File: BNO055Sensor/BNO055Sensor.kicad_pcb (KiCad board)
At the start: 4 copper layers, 50 x 35 mm, 10 parts, among them J1 locked, U1 Adafruit_BNO055_breakout

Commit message: Turns template and sensor board into two layer boards
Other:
- copper layers 4 -> 2
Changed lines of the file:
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@@
 (kicad_pcb (version 20220331) (generator pcbnew)
   (general
-    (thickness 1.6)
+    (thickness 0.57)
   )
   (paper "A4")
   (layers
     (0 "F.Cu" mixed)
-    (1 "In1.Cu" power)
-    (2 "In2.Cu" power)
     (31 "B.Cu" mixed)
-    (32 "B.Adhes" user)
-    (33 "F.Adhes" user)
+    (32 "B.Adhes" user "B.Adhesive")
+    (33 "F.Adhes" user "F.Adhesive")
     (34 "B.Paste" user)
     (35 "F.Paste" user)
-    (36 "B.SilkS" user)
-    (37 "F.SilkS" user)
+    (36 "B.SilkS" user "B.Silkscreen")
+    (37 "F.SilkS" user "F.Silkscreen")
     (38 "B.Mask" user)
     (39 "F.Mask" user)
-    (40 "Dwgs.User" user)
-    (41 "Cmts.User" user)
-    (42 "Eco1.User" user)
-    (43 "Eco2.User" user)
+    (40 "Dwgs.User" user "User.Drawings")
+    (41 "Cmts.User" user "User.Comments")
+    (42 "Eco1.User" user "User.Eco1")
+    (43 "Eco2.User" user "User.Eco2")
     (44 "Edge.Cuts" user)
     (45 "Margin" user)
-    (46 "B.CrtYd" user)
-    (47 "F.CrtYd" user)
+    (46 "B.CrtYd" user "B.Courtyard")
+    (47 "F.CrtYd" user "F.Courtyard")
     (48 "B.Fab" user)
     (49 "F.Fab" user)
@@
       (layer "F.Cu" (type "copper") (thickness 0.035))
       (layer "dielectric 1" (type "prepreg") (thickness 0.48) (material "FR4") (epsilon_r 4.5) (loss_tangent 0.02))
-      (layer "In1.Cu" (type "copper") (thickness 0.035))
-      (layer "dielectric 2" (type "prepreg") (thickness 0.48) (material "FR4") (epsilon_r 4.5) (loss_tangent 0.02))
-      (layer "In2.Cu" (type "copper") (thickness 0.035))
-      (layer "dielectric 3" (type "core") (thickness 0.48) (material "FR4") (epsilon_r 4.5) (loss_tangent 0.02))
       (layer "B.Cu" (type "copper") (thickness 0.035))
       (layer "B.Mask" (type "Bottom Solder Mask") (thickness 0.01))

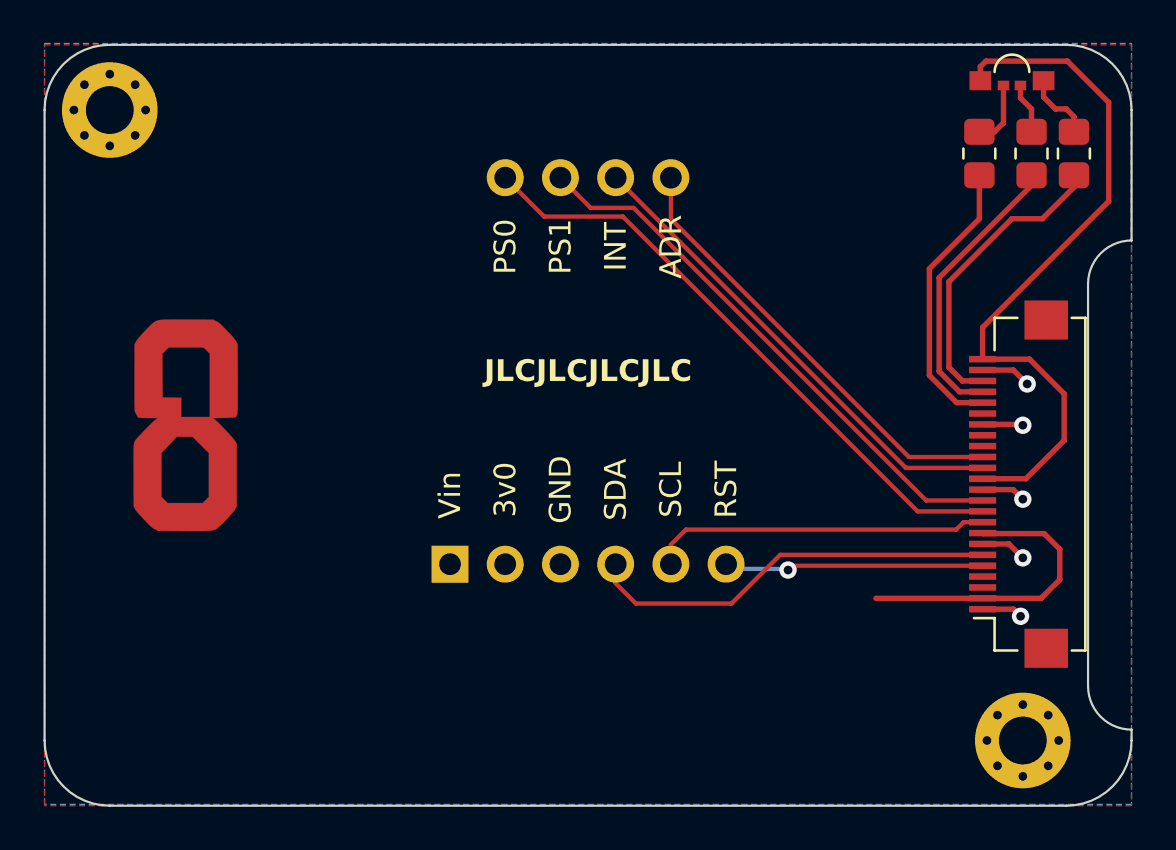
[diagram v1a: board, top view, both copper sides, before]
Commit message: Updates BNO055Sensor board after changes in the addon connector
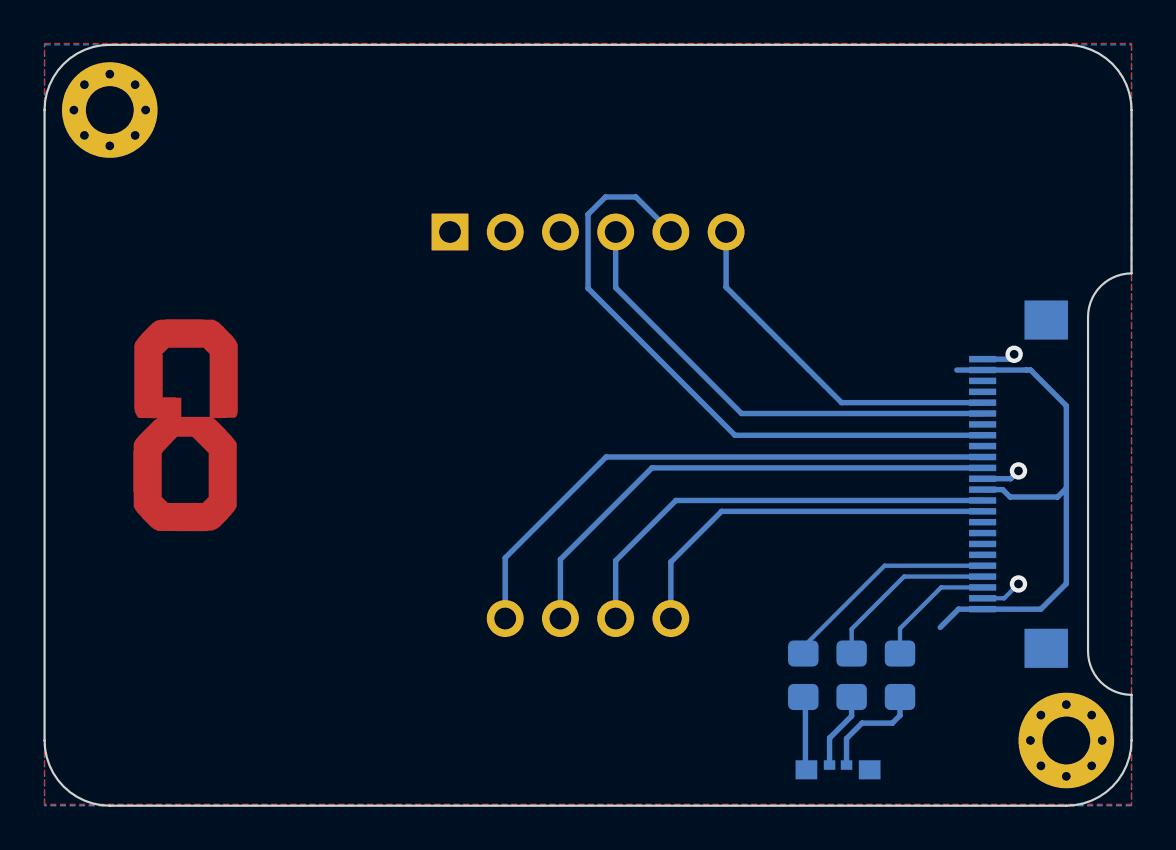
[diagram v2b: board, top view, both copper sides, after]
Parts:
- removed kibuzzard-6259E36C: G***, kibuzzard-6259E36C
- added kibuzzard-6282AB8D: G***, kibuzzard-6282AB8D, B.Cu at (122.5, 97.5)
- D1: value LED_RGBA -> LED_BGAR; moved to B.Cu
- J1: footprint GameOver:TXGA_FFC05036-24SBD113W5M_1x24_P0.50mm_Horizontal -> GameOver:Addon_conn_TXGA_FFC05036-24SBD113W5M_1x24_P0.50mm_Horizontal; moved to B.Cu
- R1, R2, R3, U1: moved to B.Cu
- moved D1 32.7 mm to (156.5, 113.3)
- moved R1 26.2 mm to (154.9, 109.0), turned to -90 degrees
- moved R3 25.3 mm to (159.3, 109.0), turned to -90 degrees
- moved R2 24.7 mm to (157.1, 109.0), turned to -90 degrees
- moved U1 5.04 mm to (145.0, 98.8)
- moved H2 2.00 mm to (167.0, 112.0)
- turned J1 to -90 degrees
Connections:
- D1 pad 1: Net-(D1-RK) -> Net-(D1-BK)
- D1 pad 3: Net-(D1-BK) -> +3V3
- D1 pad 4: +3V3 -> Net-(D1-RK)
- J1 pad 18: GND -> unconnected-(J1-IO25)
- J1 pad 20: LED_G -> LED_R
- J1 pad 21: LED_R -> LED_G
- J1 pad 7: GND -> unconnected-(J1-IO5)
- J1 pad 8: +3V3 -> SCL
- J1 pad 9: SCL -> unconnected-(J1-IO17)
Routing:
- net +3V3: track 46.8 -> 24.7 mm
- net SCL: track 15.7 -> 29.2 mm
- net LED_B: track 13.8 -> 5.73 mm
- net LED_G: track 13.1 -> 8.15 mm
- net GND: track 10.2 -> 5.27 mm, vias 5 -> 3
- net RST: track 12.0 -> 16.5 mm, vias 1 -> 0
- net LED_R: track 13.2 -> 10.1 mm
- net ADR: track 20.8 -> 17.9 mm
- net SDA: track 19.1 -> 21.8 mm
- net Net-(D1-BK): track 3.22 -> 4.97 mm
- net INT: track 22.4 -> 20.7 mm
- net PS1: track 25.6 -> 23.9 mm
- net PS0: track 28.3 -> 26.7 mm
- net Net-(D1-RK): track 2.34 -> 3.41 mm
- net Net-(D1-GK): track 3.00 -> 3.55 mm
- added copper zone on B.Cu, net +3V3
- added copper zone on F.Cu, net GND
- removed copper zone on F.Cu, net +3V3
- removed copper zone on B.Cu, net GND
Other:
- outline, holes or cut-outs redrawn

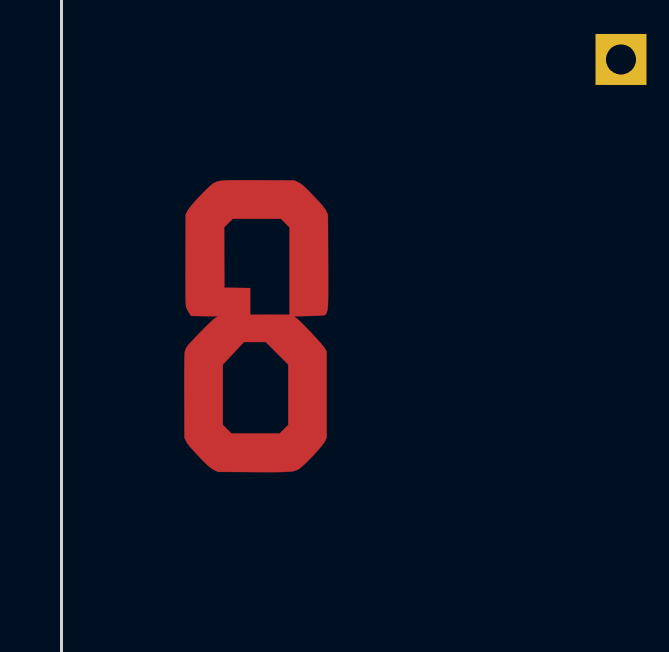
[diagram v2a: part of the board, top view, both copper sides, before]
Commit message: Fixes orientation for sensor board
The idea is to use the base board with the ESP32 facing down, and the
sensorboard with the sensor facing up. That way the connectors will face
each other correctly and the sensor will have space above (it wouldn't
fit between the boards because the battery will already be there).
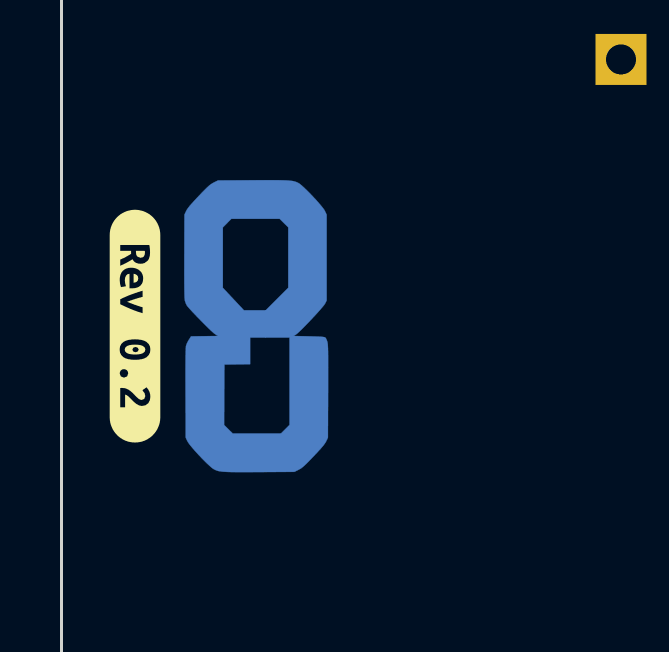
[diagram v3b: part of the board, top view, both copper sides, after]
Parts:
- Ref**: moved to B.Cu
- kibuzzard-6282AB8D: moved to F.Cu
- turned Ref** to 90 degrees
- turned kibuzzard-6282AB8D to -90 degrees

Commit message: Adds logo to BNO055 sensor board schematics
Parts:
- removed Ref**: Val**, GameOver:logo_fcu
- added LOGO1: GameOver_logo, GameOver:logo_fcu, B.Cu at (126.5, 97.4)

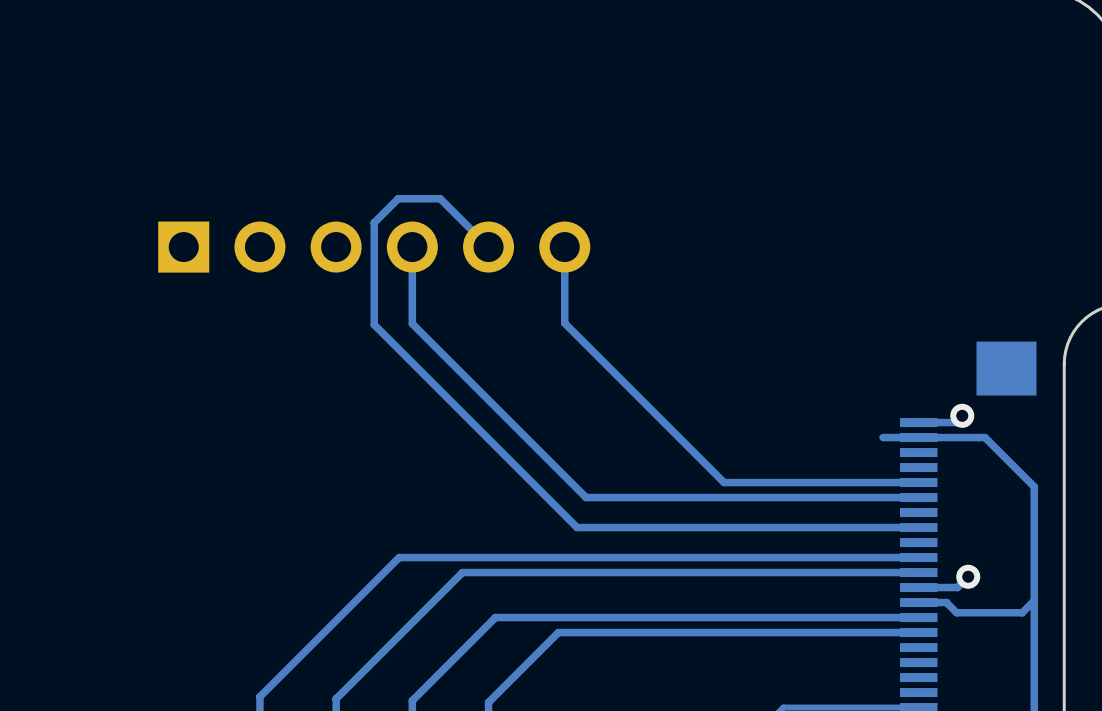
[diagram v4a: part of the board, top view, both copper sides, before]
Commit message: Updates all add-on boards with fix introduced in 692041
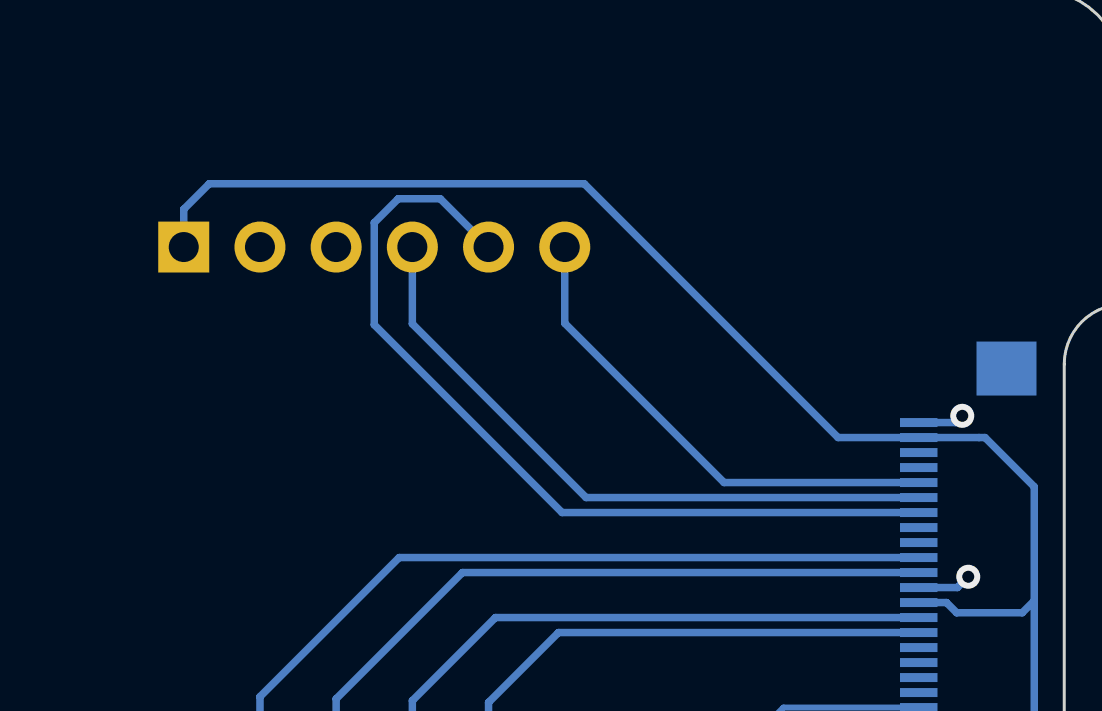
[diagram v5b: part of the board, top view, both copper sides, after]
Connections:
- J1 pad 7: unconnected-(J1-IO5) -> SCL
- J1 pad 8: SCL -> unconnected-(J1-IO5)
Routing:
- net +3V3: track 24.7 -> 53.1 mm
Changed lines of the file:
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@@
       (net 9 "SDA") (pinfunction "IO19") (pintype "bidirectional"))
     (pad "7" smd rect locked (at -2.75 1.85 270) (size 0.3 1.25) (layers "B.Cu" "B.Paste" "B.Mask")
+      (net 10 "SCL") (pinfunction "IO18") (pintype "bidirectional"))
+    (pad "8" smd rect locked (at -2.25 1.85 270) (size 0.3 1.25) (layers "B.Cu" "B.Paste" "B.Mask")
       (net 19 "unconnected-(J1-IO5)") (pinfunction "IO5") (pintype "bidirectional+no_connect"))
-    (pad "8" smd rect locked (at -2.25 1.85 270) (size 0.3 1.25) (layers "B.Cu" "B.Paste" "B.Mask")
-      (net 10 "SCL") (pinfunction "IO18") (pintype "bidirectional"))
     (pad "9" smd rect locked (at -1.75 1.85 270) (size 0.3 1.25) (layers "B.Cu" "B.Paste" "B.Mask")
       (net 24 "unconnected-(J1-IO17)") (pinfunction "IO17") (pintype "bidirectional+no_connect"))
@@
   (segment (start 167 96.6) (end 165.36 94.96) (width 0.25) (layer "B.Cu") (net 7))
   (segment (start 167 100.4) (end 167 96.6) (width 0.25) (layer "B.Cu") (net 7))
+  (segment (start 139.5 86.5) (end 138.65 87.35) (width 0.25) (layer "B.Cu") (net 7))
   (segment (start 163.15 94.96) (end 165.16 94.96) (width 0.25) (layer "B.Cu") (net 7))
   (segment (start 164.414022 100.8) (end 164.074022 100.46) (width 0.25) (layer "B.Cu") (net 7))
-  (segment (start 163.15 94.96) (end 161.96 94.96) (width 0.25) (layer "B.Cu") (net 7))
   (segment (start 164.074022 100.46) (end 163.15 100.46) (width 0.25) (layer "B.Cu") (net 7))
+  (segment (start 152 86.5) (end 139.5 86.5) (width 0.25) (layer "B.Cu") (net 7))
   (segment (start 166.6 100.8) (end 164.414022 100.8) (width 0.25) (layer "B.Cu") (net 7))
   (segment (start 165.829259 105.96) (end 167 104.789259) (width 0.25) (layer "B.Cu") (net 7))
   (segment (start 167 104.789259) (end 167 100.4) (width 0.25) (layer "B.Cu") (net 7))
   (segment (start 163.15 105.96) (end 165.829259 105.96) (width 0.25) (layer "B.Cu") (net 7))
+  (segment (start 160.46 94.96) (end 152 86.5) (width 0.25) (layer "B.Cu") (net 7))
   (segment (start 162.04 105.96) (end 161.2 106.8) (width 0.25) (layer "B.Cu") (net 7))
+  (segment (start 163.15 94.96) (end 160.46 94.96) (width 0.25) (layer "B.Cu") (net 7))
+  (segment (start 138.65 87.35) (end 138.65 88.61) (width 0.25) (layer "B.Cu") (net 7))
   (segment (start 163.15 105.96) (end 162.04 105.96) (width 0.25) (layer "B.Cu") (net 7))
   (segment (start 165.36 94.96) (end 165.16 94.96) (width 0.25) (layer "B.Cu") (net 7))
@@
   (segment (start 146.27 88.61) (end 146.27 91.17) (width 0.25) (layer "B.Cu") (net 9))
   (segment (start 152.06 96.96) (end 163.15 96.96) (width 0.25) (layer "B.Cu") (net 9))
-  (segment (start 163.15 97.96) (end 151.76 97.96) (width 0.25) (layer "B.Cu") (net 10))
+  (segment (start 145.8 87) (end 147.2 87) (width 0.25) (layer "B.Cu") (net 10))
   (segment (start 145 91.2) (end 145 87.8) (width 0.25) (layer "B.Cu") (net 10))
+  (segment (start 147.2 87) (end 148.81 88.61) (width 0.25) (layer "B.Cu") (net 10))
+  (segment (start 151.26 97.46) (end 145 91.2) (width 0.25) (layer "B.Cu") (net 10))
   (segment (start 145 87.8) (end 145.8 87) (width 0.25) (layer "B.Cu") (net 10))
-  (segment (start 151.76 97.96) (end 145 91.2) (width 0.25) (layer "B.Cu") (net 10))
-  (segment (start 147.2 87) (end 148.81 88.61) (width 0.25) (layer "B.Cu") (net 10))
-  (segment (start 145.8 87) (end 147.2 87) (width 0.25) (layer "B.Cu") (net 10))
+  (segment (start 163.15 97.46) (end 151.26 97.46) (width 0.25) (layer "B.Cu") (net 10))
   (segment (start 163.15 98.96) (end 145.83 98.96) (width 0.25) (layer "B.Cu") (net 11))
   (segment (start 145.83 98.96) (end 141.19 103.6) (width 0.25) (layer "B.Cu") (net 11))

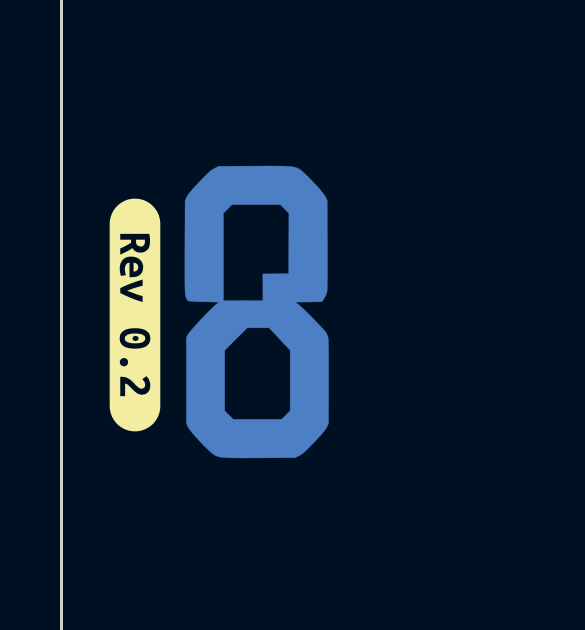
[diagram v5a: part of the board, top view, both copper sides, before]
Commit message: Update version label on PCBs to 1.0
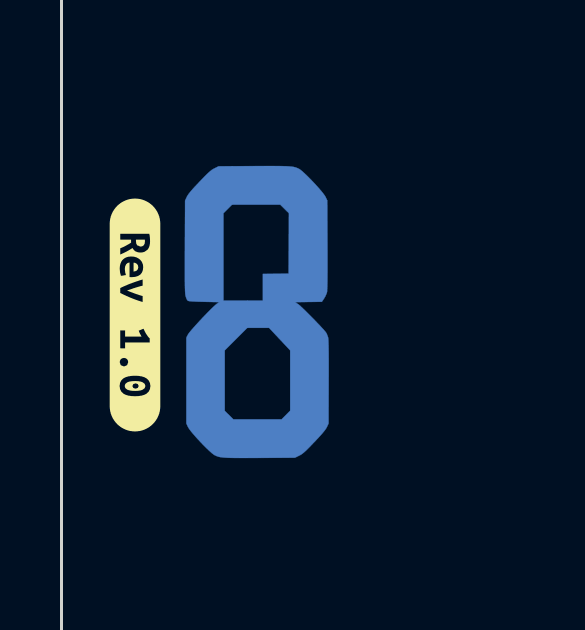
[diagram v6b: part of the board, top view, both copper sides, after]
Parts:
- removed kibuzzard-6282AB8D: G***, kibuzzard-6282AB8D
- added kibuzzard-63029CE8: G***, kibuzzard-63029CE8, F.Cu at (122.5, 97.5)
